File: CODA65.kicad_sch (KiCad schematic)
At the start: 24 parts, among them J1 Conn_01x04, J2 Conn_01x05, SW1 SW_Push, SW2 SW_Push, U1 RP2040, U2 W25Q128JVS, Y1 Crystal_GND24

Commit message: Finished switch matrix
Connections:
- net ROT A: now reaches U1.40 (GPIO28_ADC2)
- net ROT B: now reaches U1.41 (GPIO29_ADC3)
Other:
- added sheet LED Shit (untitled.kicad_sch)
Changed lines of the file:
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@@
+    )
+  )
+  (global_label "ROT A" (shape input) (at 247.65 128.27 0) (fields_autoplaced)
+    (effects (font (size 1.27 1.27)) (justify left))
+    (property "Intersheetrefs" "${INTERSHEET_REFS}" (at 256.2595 128.27 0)
+      (effects (font (size 1.27 1.27)) (justify left) hide)
     )
   )
@@
     (property "Intersheetrefs" "${INTERSHEET_REFS}" (at 188.4219 82.55 0)
       (effects (font (size 1.27 1.27)) (justify right) hide)
+    )
+  )
+  (global_label "ROT B" (shape input) (at 247.65 130.81 0) (fields_autoplaced)
+    (effects (font (size 1.27 1.27)) (justify left))
+    (property "Intersheetrefs" "${INTERSHEET_REFS}" (at 256.4409 130.81 0)
+      (effects (font (size 1.27 1.27)) (justify left) hide)
     )
   )
@@
     )
   )
-  (sheet (at 35.56 144.78) (size 69.85 46.99) (fields_autoplaced)
+  (sheet (at 88.9 146.05) (size 78.74 46.99) (fields_autoplaced)
     (stroke (width 0.1524) (type solid))
     (fill (color 0 0 0 0.0000))
-    (property "Sheetname" "Matrix" (at 35.56 144.0684 0)
+    (property "Sheetname" "LED Shit" (at 88.9 145.3384 0)
       (effects (font (size 1.27 1.27)) (justify left bottom))
     )
-    (property "Sheetfile" "Matrix.kicad_sch" (at 35.56 192.3546 0)
+    (property "Sheetfile" "untitled.kicad_sch" (at 88.9 193.6246 0)
       (effects (font (size 1.27 1.27)) (justify left top))
     )
+    (instances
+      (project "CODA65"
+        (path "/33ce4dbb-1d04-4b2d-9cde-6cc03c168fa4" (page "3"))
+      )
+    )
+  )
+  (sheet (at 13.97 146.05) (size 69.85 46.99) (fields_autoplaced)
+    (stroke (width 0.1524) (type solid))
+    (fill (color 0 0 0 0.0000))
+    (property "Sheetname" "Matrix" (at 13.97 145.3384 0)
+      (effects (font (size 1.27 1.27)) (justify left bottom))
+    )
+    (property "Sheetfile" "Matrix.kicad_sch" (at 13.97 193.6246 0)
+      (effects (font (size 1.27 1.27)) (justify left top))
+    )

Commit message: idk
dont remember what i changed lol i think it should be led shit
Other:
- sheet LED Shit: file untitled.kicad_sch -> LEDShit.kicad_sch
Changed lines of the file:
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@@
       (effects (font (size 1.27 1.27)) (justify left bottom))
     )
-    (property "Sheetfile" "untitled.kicad_sch" (at 88.9 193.6246 0)
+    (property "Sheetfile" "LEDShit.kicad_sch" (at 88.9 193.6246 0)
       (effects (font (size 1.27 1.27)) (justify left top))
     )

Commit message: Led Matrix stuf
need to get a better idea of power/data reqs
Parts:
- added R8: 0.5k, symbol Device:R_Small
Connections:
- net at U1.39 (GPIO27_ADC1): now also R8.1
- new net LED_DATA: R8.2
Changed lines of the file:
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@@
   (junction (at 243.84 33.02) (diameter 0) (color 0 0 0 0)
   )
+  (wire (pts (xy 250.19 125.73) (xy 247.65 125.73))
+    (stroke (width 0) (type default))
+  )
   (wire (pts (xy 63.5 90.17) (xy 67.31 90.17))
     (stroke (width 0) (type default))
@@
   )
   (wire (pts (xy 129.54 115.57) (xy 129.54 113.03))
+    (stroke (width 0) (type default))
+  )
+  (wire (pts (xy 257.81 125.73) (xy 255.27 125.73))
     (stroke (width 0) (type default))
   )
@@
     (property "Intersheetrefs" "${INTERSHEET_REFS}" (at 188.1801 72.39 0)
       (effects (font (size 1.27 1.27)) (justify right) hide)
+    )
+  )
+  (global_label "LED_DATA" (shape input) (at 257.81 125.73 0) (fields_autoplaced)
+    (effects (font (size 1.27 1.27)) (justify left))
+    (property "Intersheetrefs" "${INTERSHEET_REFS}" (at 269.6247 125.73 0)
+      (effects (font (size 1.27 1.27)) (justify left) hide)
     )
   )
@@
         )
       )
+    )
+  )
+  (symbol (lib_id "Device:R_Small") (at 252.73 125.73 90) (unit 1)
+    (in_bom yes) (on_board yes) (dnp no) (fields_autoplaced)
+    (property "Reference" "R8" (at 252.73 120.65 90)
+      (effects (font (size 1.27 1.27)))
+    )
+    (property "Value" "0.5k" (at 252.73 123.19 90)
+      (effects (font (size 1.27 1.27)))
+    )
+    (property "Footprint" "" (at 252.73 125.73 0)
+      (effects (font (size 1.27 1.27)) hide)
+    )
+    (property "Datasheet" "~" (at 252.73 125.73 0)
+      (effects (font (size 1.27 1.27)) hide)
+    )
+    (pin "1")
+    (pin "2")
+    (instances
+      (project "CODA65"
+        (path "/33ce4dbb-1d04-4b2d-9cde-6cc03c168fa4"
+          (reference "R8") (unit 1)
+        )
+      )

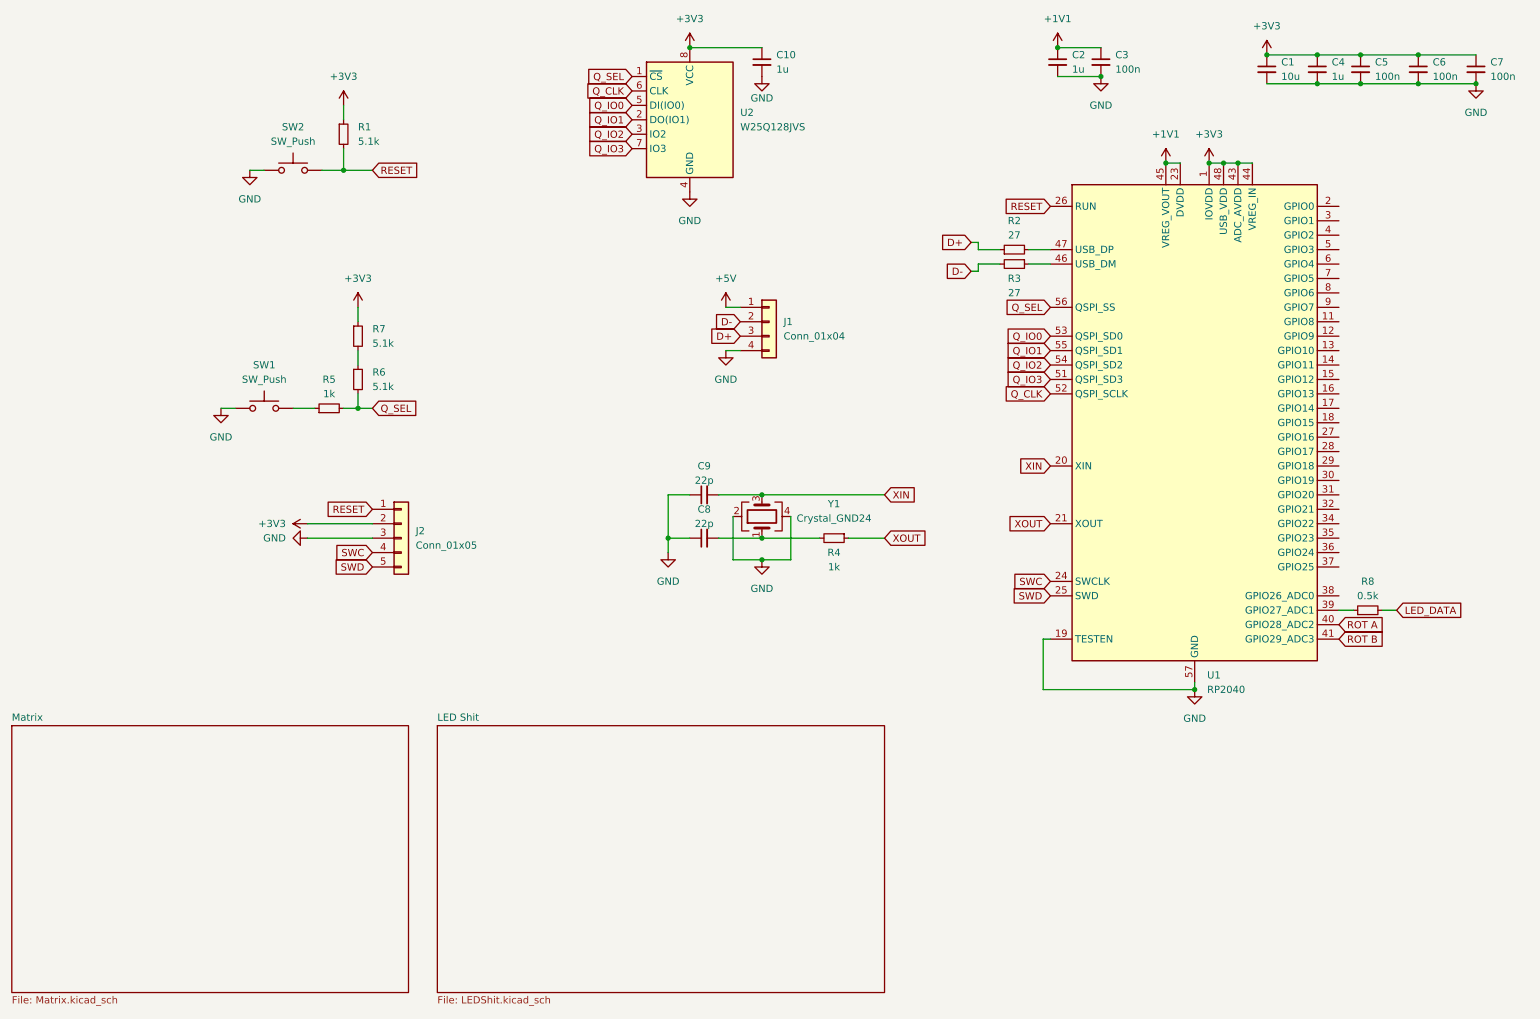
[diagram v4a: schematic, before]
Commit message: Finished LED matrix
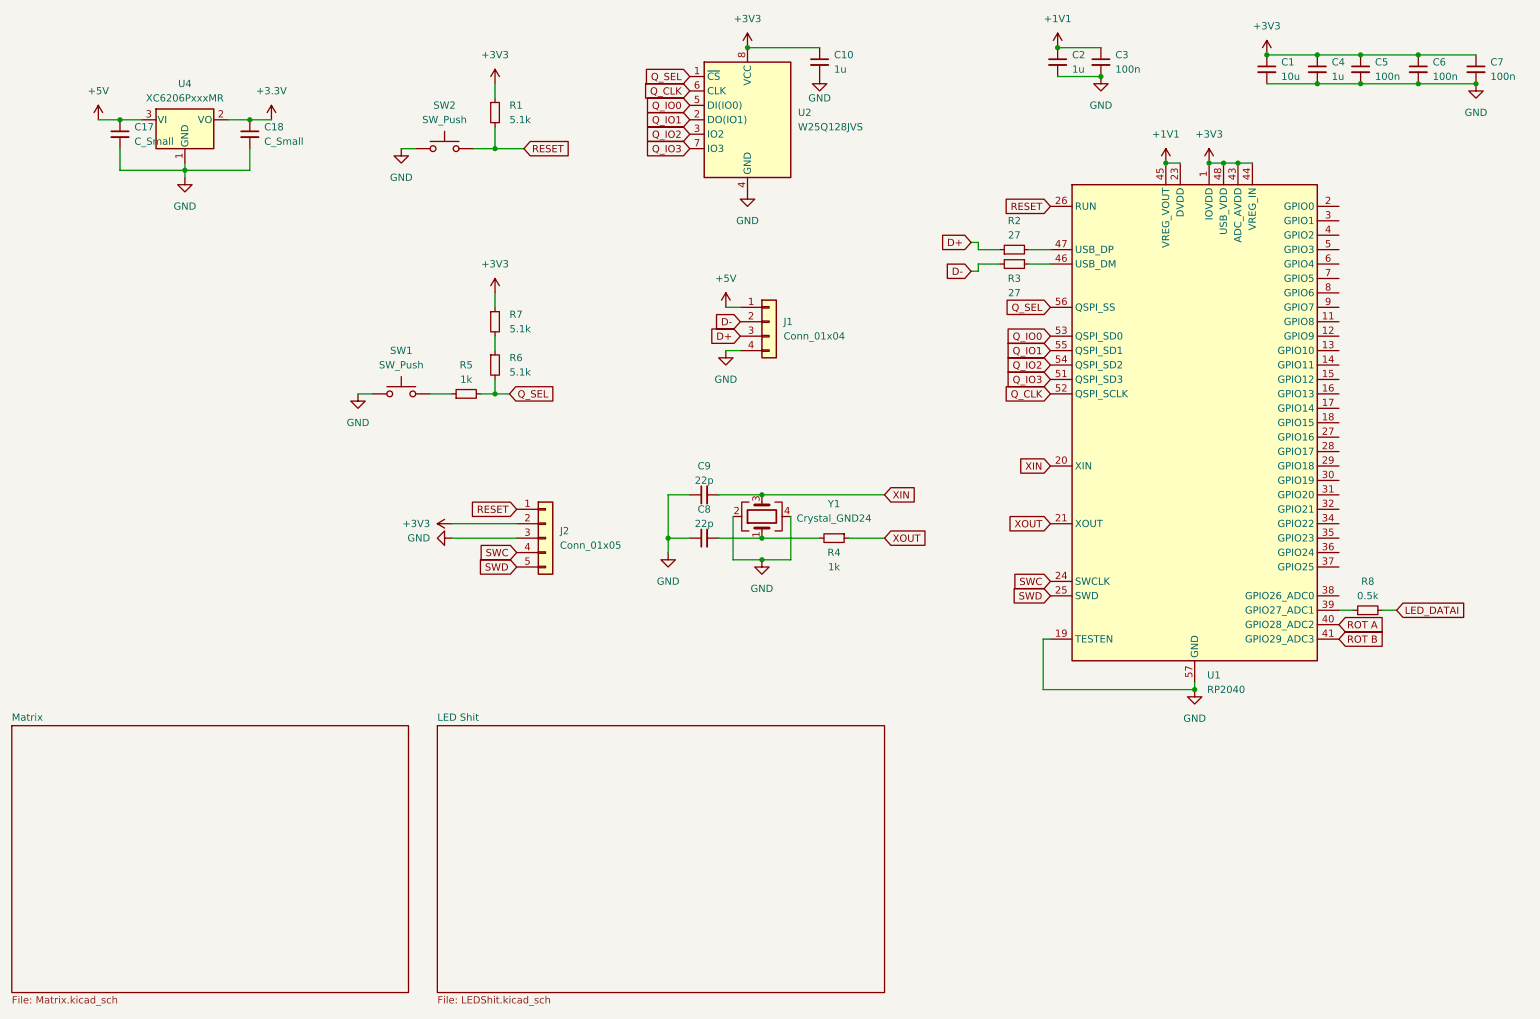
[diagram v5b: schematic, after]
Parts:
- added C17, C18: C_Small, symbol Device:C_Small
- added U4: XC6206PxxxMR, Package_TO_SOT_SMD:SOT-23-3, symbol Regulator_Linear:XC6206PxxxMR
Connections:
- net +5V: now also C17.1, U4.3 (VI)
- net GND: now also C17.2, C18.2, U4.1 (GND)
- net LED_DATA renamed LED_DATAI
- new net +3.3V: C18.1, U4.2 (VO)
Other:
- moved on the sheet: C10, J2, R1, R5, R6, R7, SW1, SW2, U2

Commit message: assigned schema
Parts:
- C1: value 10u -> 10uF; footprint (none) -> Capacitor_SMD:C_0603_1608Metric
- C10, C2, C4: value 1u -> 1uF; footprint (none) -> Capacitor_SMD:C_0402_1005Metric
- C17, C18: value C_Small -> 1uF; footprint (none) -> Capacitor_SMD:C_0402_1005Metric
- C3, C5, C6, C7: value 100n -> 100nF; footprint (none) -> Capacitor_SMD:C_0402_1005Metric
- C8, C9: value 22p -> 22pF; footprint (none) -> Capacitor_SMD:C_0402_1005Metric
- J1: footprint (none) -> Connector_JST:JST_SH_SM04B-SRSS-TB_1x04-1MP_P1.00mm_Horizontal
- J2: footprint (none) -> Connector_PinHeader_2.54mm:PinHeader_1x05_P2.54mm_Vertical
- R1, R2, R3, R4, R5, R6, R7, R8: footprint (none) -> Resistor_SMD:R_0402_1005Metric
- SW1, SW2: footprint (none) -> Button_Switch_SMD:SW_Push_1P1T_XKB_TS-1187A
- Y1: footprint (none) -> Crystal:Crystal_SMD_3225-4Pin_3.2x2.5mm
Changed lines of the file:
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@@
       (effects (font (size 1.27 1.27)) (justify left))
     )
-    (property "Footprint" "" (at 147.32 74.93 0)
+    (property "Footprint" "Connector_JST:JST_SH_SM04B-SRSS-TB_1x04-1MP_P1.00mm_Horizontal" (at 147.32 74.93 0)
       (effects (font (size 1.27 1.27)) hide)
     )
@@
       (effects (font (size 1.27 1.27)) (justify left))
     )
-    (property "Value" "1u" (at 158.75 30.4863 0)
-      (effects (font (size 1.27 1.27)) (justify left))
-    )
-    (property "Footprint" "" (at 156.21 29.21 0)
+    (property "Value" "1uF" (at 158.75 30.4863 0)
+      (effects (font (size 1.27 1.27)) (justify left))
+    )
+    (property "Footprint" "Capacitor_SMD:C_0402_1005Metric" (at 156.21 29.21 0)
       (effects (font (size 1.27 1.27)) hide)
     )
@@
       (effects (font (size 1.27 1.27)) (justify left))
     )
-    (property "Footprint" "" (at 99.06 74.93 0)
+    (property "Footprint" "Resistor_SMD:R_0402_1005Metric" (at 99.06 74.93 0)
       (effects (font (size 1.27 1.27)) hide)
     )
@@
       (effects (font (size 1.27 1.27)) (justify left))
     )
-    (property "Value" "100n" (at 208.28 30.4863 0)
-      (effects (font (size 1.27 1.27)) (justify left))
-    )
-    (property "Footprint" "" (at 205.74 29.21 0)
+    (property "Value" "100nF" (at 208.28 30.4863 0)
+      (effects (font (size 1.27 1.27)) (justify left))
+    )
+    (property "Footprint" "Capacitor_SMD:C_0402_1005Metric" (at 205.74 29.21 0)
       (effects (font (size 1.27 1.27)) hide)
     )
@@
       (effects (font (size 1.27 1.27)))
     )
-    (property "Footprint" "" (at 90.17 39.37 0)
+    (property "Footprint" "Button_Switch_SMD:SW_Push_1P1T_XKB_TS-1187A" (at 90.17 39.37 0)
       (effects (font (size 1.27 1.27)) hide)
     )
@@
       (effects (font (size 1.27 1.27)) (justify left))
     )
-    (property "Footprint" "" (at 99.06 38.1 0)
+    (property "Footprint" "Resistor_SMD:R_0402_1005Metric" (at 99.06 38.1 0)
       (effects (font (size 1.27 1.27)) hide)
     )
@@
       (effects (font (size 1.27 1.27)))
     )
-    (property "Footprint" "" (at 158.75 113.03 0)
+    (property "Footprint" "Resistor_SMD:R_0402_1005Metric" (at 158.75 113.03 0)
       (effects (font (size 1.27 1.27)) hide)
     )
@@
       (effects (font (size 1.27 1.27)) (justify left))
     )
-    (property "Value" "10u" (at 237.49 31.7563 0)
-      (effects (font (size 1.27 1.27)) (justify left))
-    )
-    (property "Footprint" "" (at 234.95 30.48 0)
+    (property "Value" "10uF" (at 237.49 31.7563 0)
+      (effects (font (size 1.27 1.27)) (justify left))
+    )
+    (property "Footprint" "Capacitor_SMD:C_0603_1608Metric" (at 234.95 30.48 0)
       (effects (font (size 1.27 1.27)) hide)
     )
@@
       (effects (font (size 1.27 1.27)) (justify left))
     )
-    (property "Value" "1u" (at 200.66 30.4863 0)
-      (effects (font (size 1.27 1.27)) (justify left))
-    )
-    (property "Footprint" "" (at 198.12 29.21 0)
+    (property "Value" "1uF" (at 200.66 30.4863 0)
+      (effects (font (size 1.27 1.27)) (justify left))
+    )
+    (property "Footprint" "Capacitor_SMD:C_0402_1005Metric" (at 198.12 29.21 0)
       (effects (font (size 1.27 1.27)) hide)
     )
@@
       (effects (font (size 1.27 1.27)) (justify left))
     )
-    (property "Value" "C_Small" (at 58.42 43.1863 0)
-      (effects (font (size 1.27 1.27)) (justify left))
-    )
-    (property "Footprint" "" (at 55.88 41.91 0)
+    (property "Value" "1uF" (at 58.42 43.1863 0)
+      (effects (font (size 1.27 1.27)) (justify left))
+    )
+    (property "Footprint" "Capacitor_SMD:C_0402_1005Metric" (at 55.88 41.91 0)
       (effects (font (size 1.27 1.27)) hide)
     )
@@
       (effects (font (size 1.27 1.27)))
     )
-    (property "Footprint" "" (at 190.5 62.23 0)
+    (property "Footprint" "Resistor_SMD:R_0402_1005Metric" (at 190.5 62.23 0)
       (effects (font (size 1.27 1.27)) hide)
     )
@@
       (effects (font (size 1.27 1.27)) (justify left))
     )
-    (property "Value" "C_Small" (at 35.56 43.1863 0)
-      (effects (font (size 1.27 1.27)) (justify left))
-    )
-    (property "Footprint" "" (at 33.02 41.91 0)
+    (property "Value" "1uF" (at 35.56 43.1863 0)
+      (effects (font (size 1.27 1.27)) (justify left))
+    )
+    (property "Footprint" "Capacitor_SMD:C_0402_1005Metric" (at 33.02 41.91 0)
       (effects (font (size 1.27 1.27)) hide)
     )
@@
       (effects (font (size 1.27 1.27)))
     )
-    (property "Footprint" "" (at 146.05 109.22 0)
+    (property "Footprint" "Crystal:Crystal_SMD_3225-4Pin_3.2x2.5mm" (at 146.05 109.22 0)
       (effects (font (size 1.27 1.27)) hide)
     )
@@
       (effects (font (size 1.27 1.27)))
     )
-    (property "Footprint" "" (at 82.55 82.55 0)
+    (property "Footprint" "Button_Switch_SMD:SW_Push_1P1T_XKB_TS-1187A" (at 82.55 82.55 0)
       (effects (font (size 1.27 1.27)) hide)
     )
@@
       (effects (font (size 1.27 1.27)))
     )
-    (property "Value" "22p" (at 135.89 110.49 90)
-      (effects (font (size 1.27 1.27)))
-    )
-    (property "Footprint" "" (at 135.89 113.03 0)
+    (property "Value" "22pF" (at 135.89 110.49 90)
+      (effects (font (size 1.27 1.27)))
+    )
+    (property "Footprint" "Capacitor_SMD:C_0402_1005Metric" (at 135.89 113.03 0)
       (effects (font (size 1.27 1.27)) hide)
     )
@@
       (effects (font (size 1.27 1.27)))
     )
-    (property "Footprint" "" (at 252.73 125.73 0)
+    (property "Footprint" "Resistor_SMD:R_0402_1005Metric" (at 252.73 125.73 0)
       (effects (font (size 1.27 1.27)) hide)
     )
@@
       (effects (font (size 1.27 1.27)) (justify left))
     )
-    (property "Footprint" "" (at 99.06 82.55 0)
+    (property "Footprint" "Resistor_SMD:R_0402_1005Metric" (at 99.06 82.55 0)
       (effects (font (size 1.27 1.27)) hide)
     )
@@
       (effects (font (size 1.27 1.27)))
     )
-    (property "Value" "22p" (at 135.89 102.87 90)
-      (effects (font (size 1.27 1.27)))
-    )
-    (property "Footprint" "" (at 135.89 105.41 0)
+    (property "Value" "22pF" (at 135.89 102.87 90)
+      (effects (font (size 1.27 1.27)))
+    )
+    (property "Footprint" "Capacitor_SMD:C_0402_1005Metric" (at 135.89 105.41 0)
       (effects (font (size 1.27 1.27)) hide)
     )
@@
       (effects (font (size 1.27 1.27)) (justify left))
     )
-    (property "Value" "100n" (at 274.32 31.7563 0)
-      (effects (font (size 1.27 1.27)) (justify left))
-    )
-    (property "Footprint" "" (at 271.78 30.48 0)
+    (property "Value" "100nF" (at 274.32 31.7563 0)
+      (effects (font (size 1.27 1.27)) (justify left))
+    )
+    (property "Footprint" "Capacitor_SMD:C_0402_1005Metric" (at 271.78 30.48 0)
       (effects (font (size 1.27 1.27)) hide)
     )
@@
       (effects (font (size 1.27 1.27)) (justify left))
     )
-    (property "Value" "100n" (at 254 31.7563 0)
-      (effects (font (size 1.27 1.27)) (justify left))
-    )
-    (property "Footprint" "" (at 251.46 30.48 0)
+    (property "Value" "100nF" (at 254 31.7563 0)
+      (effects (font (size 1.27 1.27)) (justify left))
+    )
+    (property "Footprint" "Capacitor_SMD:C_0402_1005Metric" (at 251.46 30.48 0)
       (effects (font (size 1.27 1.27)) hide)
     )
@@
       (effects (font (size 1.27 1.27)))
     )
-    (property "Footprint" "" (at 93.98 87.63 0)
+    (property "Footprint" "Resistor_SMD:R_0402_1005Metric" (at 93.98 87.63 0)
       (effects (font (size 1.27 1.27)) hide)
     )
@@
       (effects (font (size 1.27 1.27)))
     )
-    (property "Footprint" "" (at 190.5 64.77 0)
+    (property "Footprint" "Resistor_SMD:R_0402_1005Metric" (at 190.5 64.77 0)
       (effects (font (size 1.27 1.27)) hide)
     )
@@
       (effects (font (size 1.27 1.27)) (justify left))
     )
-    (property "Footprint" "" (at 107.95 113.03 0)
+    (property "Footprint" "Connector_PinHeader_2.54mm:PinHeader_1x05_P2.54mm_Vertical" (at 107.95 113.03 0)
       (effects (font (size 1.27 1.27)) hide)
     )
@@
       (effects (font (size 1.27 1.27)) (justify left))
     )
-    (property "Value" "1u" (at 246.38 31.7563 0)
-      (effects (font (size 1.27 1.27)) (justify left))
-    )
-    (property "Footprint" "" (at 243.84 30.48 0)
+    (property "Value" "1uF" (at 246.38 31.7563 0)
+      (effects (font (size 1.27 1.27)) (justify left))
+    )
+    (property "Footprint" "Capacitor_SMD:C_0402_1005Metric" (at 243.84 30.48 0)
       (effects (font (size 1.27 1.27)) hide)
     )
@@
       (effects (font (size 1.27 1.27)) (justify left))
     )
-    (property "Value" "100n" (at 264.16 31.7563 0)
-      (effects (font (size 1.27 1.27)) (justify left))
-    )
-    (property "Footprint" "" (at 261.62 30.48 0)
-      (effects (font (size 1.27 1.27)) hide)
-    )
+    (property "Value" "100nF" (at 264.16 31.7563 0)
+      (effects (font (size 1.27 1.27)) (justify left))
+    )
+    (property "Footprint" "Capacitor_SMD:C_0402_1005Metric" (at 261.62 30.48 0)
+      (effects (font (size 1.27 1.27)) hide)
+    )
